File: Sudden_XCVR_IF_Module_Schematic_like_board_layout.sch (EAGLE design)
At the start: 31 parts, among them K1 REL-G5V1, K2 REL-G5V1, K3 RELAY-DPDT

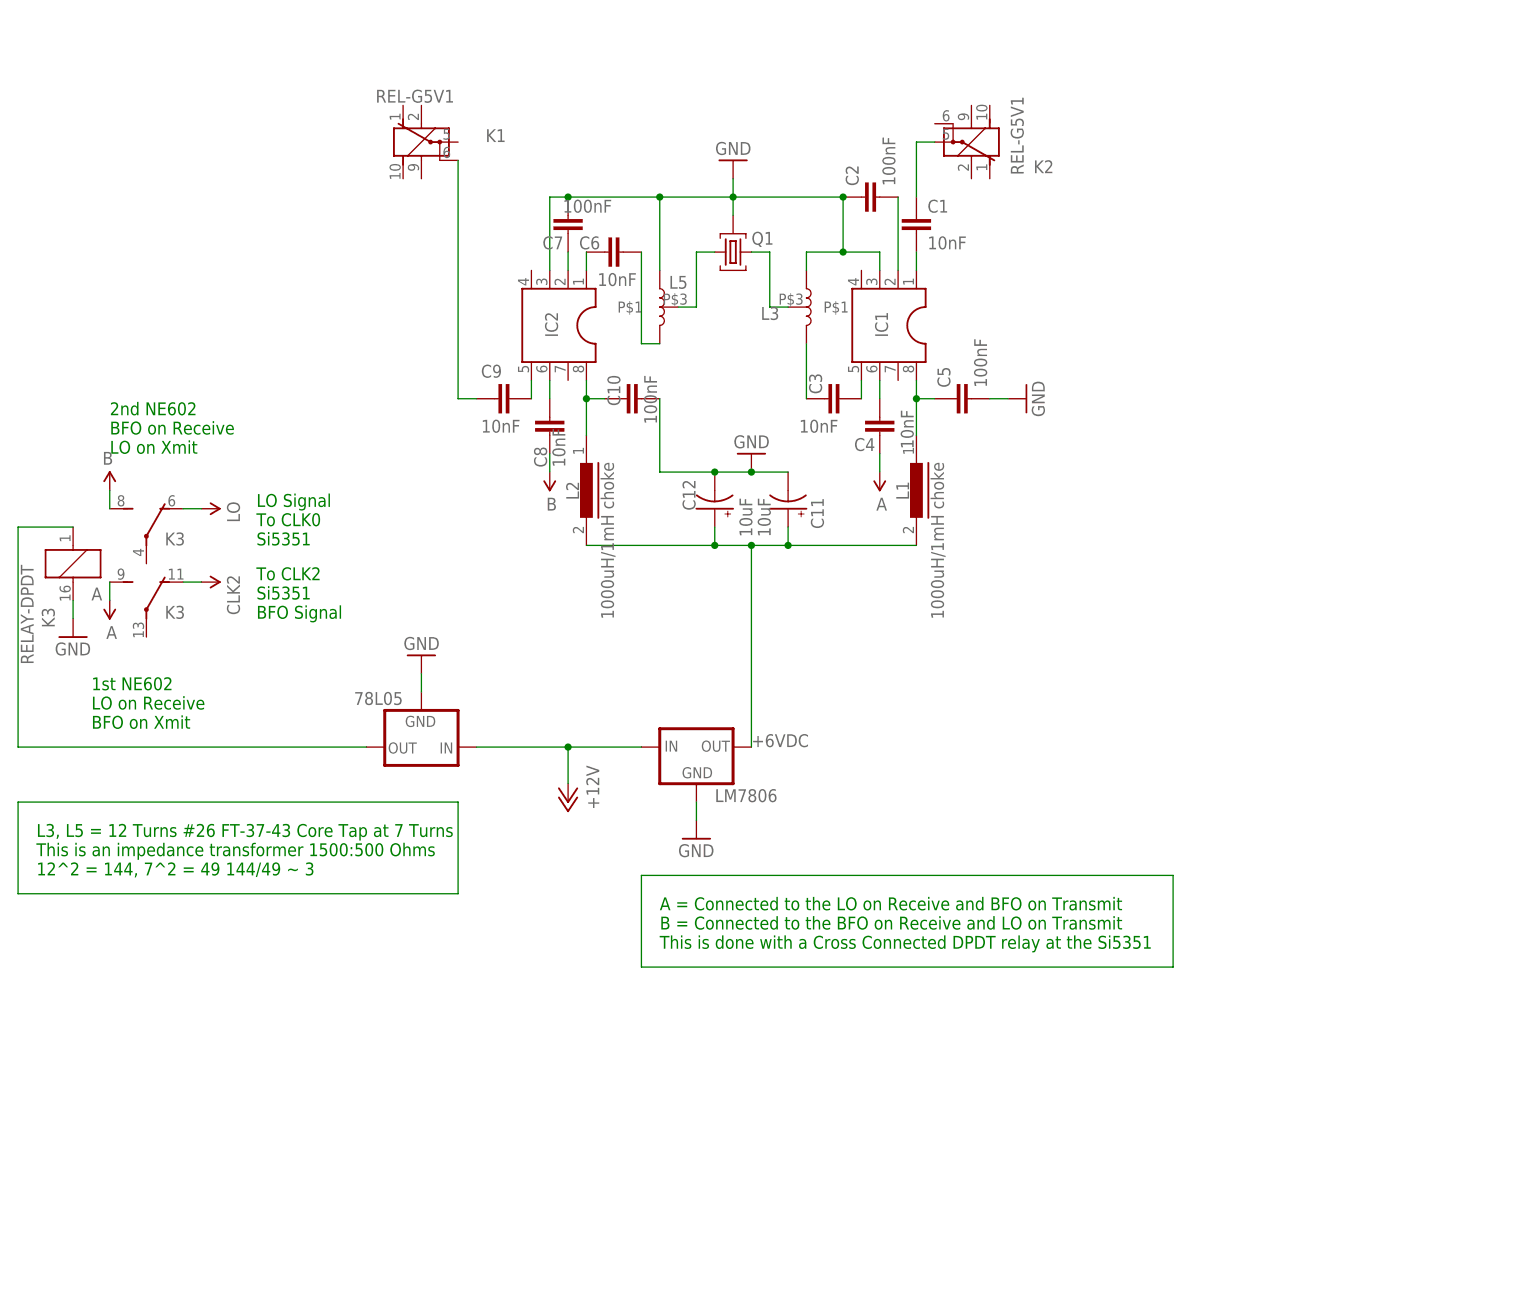
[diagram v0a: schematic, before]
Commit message: Added additional schematics and board layout
Added additional schmentics and board layout for Driver stage and a new IF schematic and board
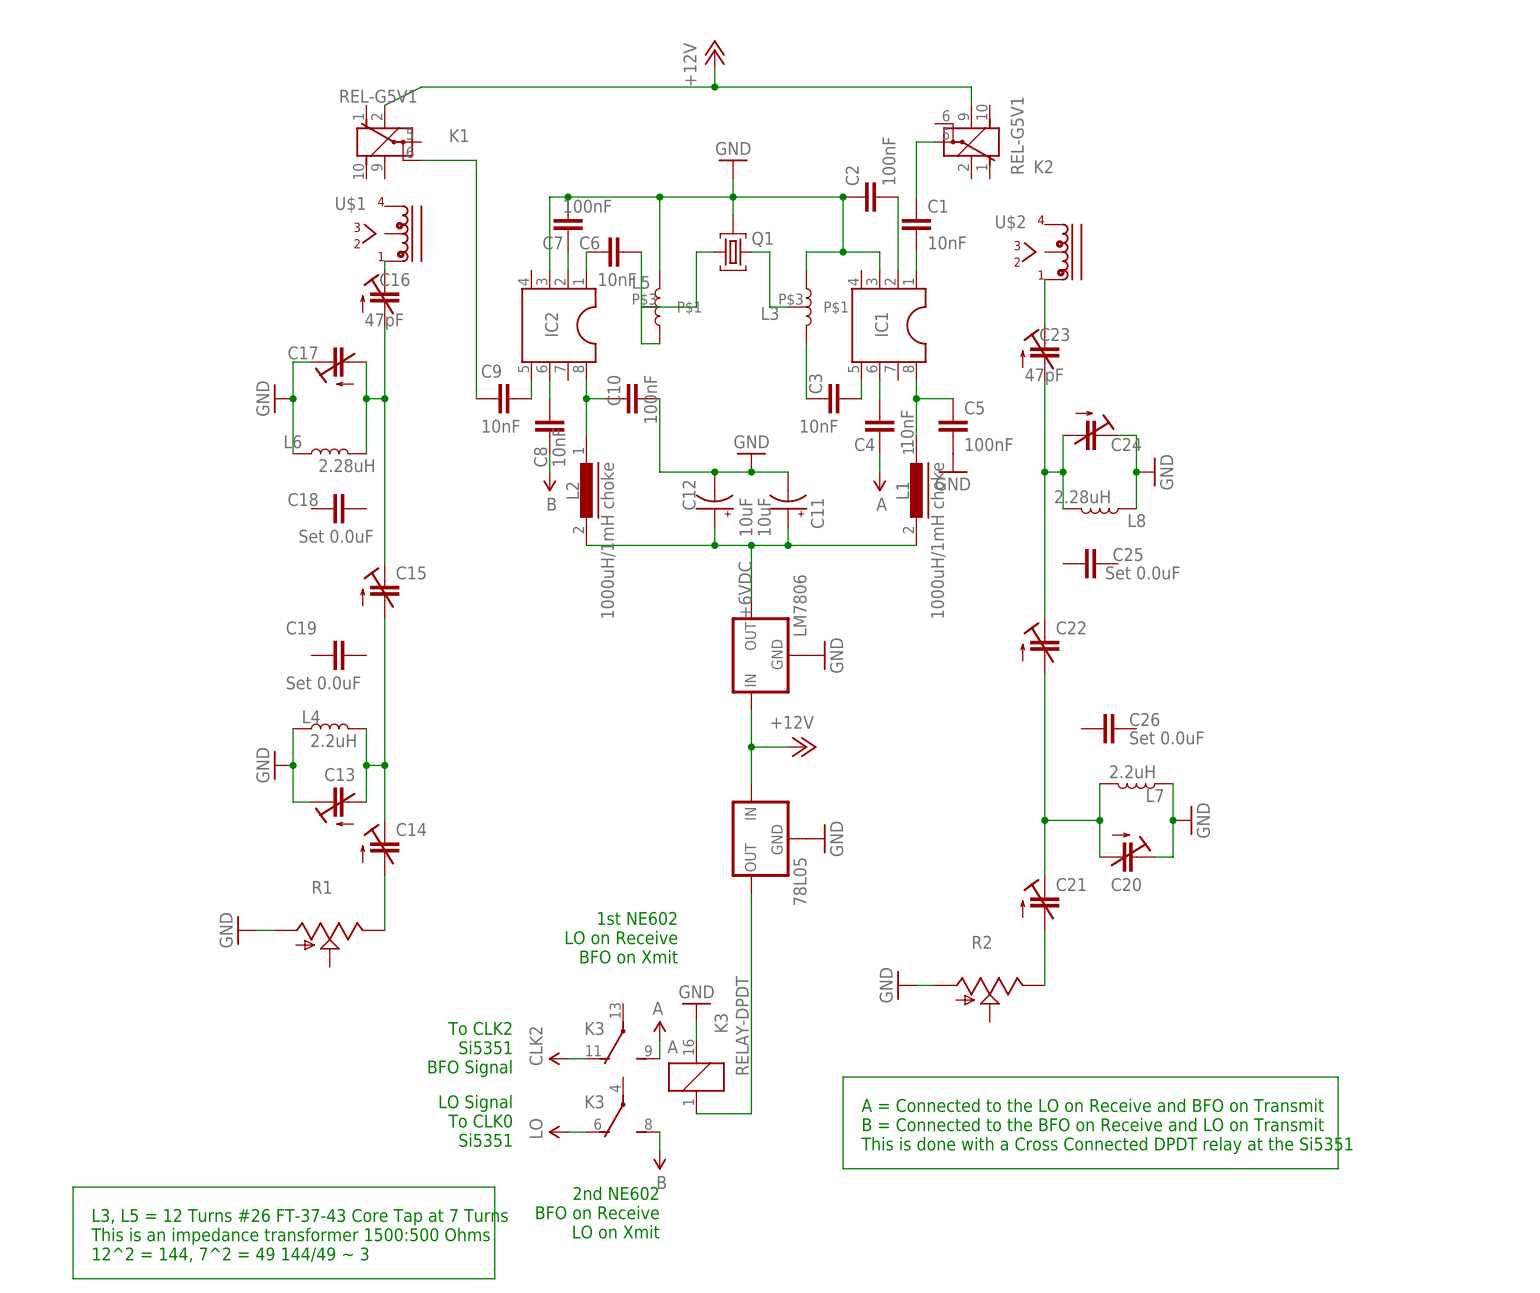
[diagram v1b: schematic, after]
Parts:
- added C13, C14, C15, C17, C20, C21, C22, C24: (no value), jim_muppet_parts:CAP-TRIMM3008
- added C16, C23: 47pF, jim_muppet_parts:CAP-TRIMM3008
- added C18, C19, C25, C26: Set 0.0uF, jim_muppet_parts:CAP-MEDIUM-MUPPET
- added L4, L7: 2.2uH, jim_muppet_parts:INDUCTOR-VLF4012AT-2.2UH
- added L6, L8: 2.28uH, jim_muppet_parts:INDUCTOR-VLF4012AT-2.2UH
- added P+2: +12V, jim_muppet_parts:+12V
- added R1, R2: (no value), jim_muppet_parts:POTENTIOMETER-TRIMCT6
- added U$1: T37-43_BIFILAR_TORIODBIFILAR-COIL/TRANSFORMER, jim_muppet_parts:T37-43_BIFILAR_TORIODBIFILAR-COIL/TRANSFORMER
- added U$2: BIFILAR_TORIOD, jim_muppet_parts:T37-43_BIFILAR_TORIODBIFILAR-COIL/TRANSFORMER
- L5: value INDUCTOR-TAPPED-MIRROREDINDUCTOR_TAPPED_MIRRORED -> INDUCTOR-TAPPED
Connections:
- new net N$21: C15.E, C16.A, C17.A, L6.2
- new net N$22: C14.A, R1.E
- new net N$23: C13.A, C14.E, C15.A, L4.2
- new net N$24: C23.E, U$2.C1A
- new net N$25: C22.E, C23.A, C24.A, L8.2
- new net N$26: C20.A, C21.E, C22.A, L7.2
- new net N$27: C21.A, R2.E
- new net N$8: C16.E, U$1.C1A
- net +12V: now also K11.1, K21.2, P+2.+12V
- net GND: now also C13.E, C17.E, C20.E, C24.E, L4.1, L6.1, L7.1, L8.1, R1.A, R2.A
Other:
- moved on the sheet: 78L05, C5, K1, K3, L5, LM7806

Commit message: Updated the IF module - mainly board layout
Updated the IF module - mainly board layout
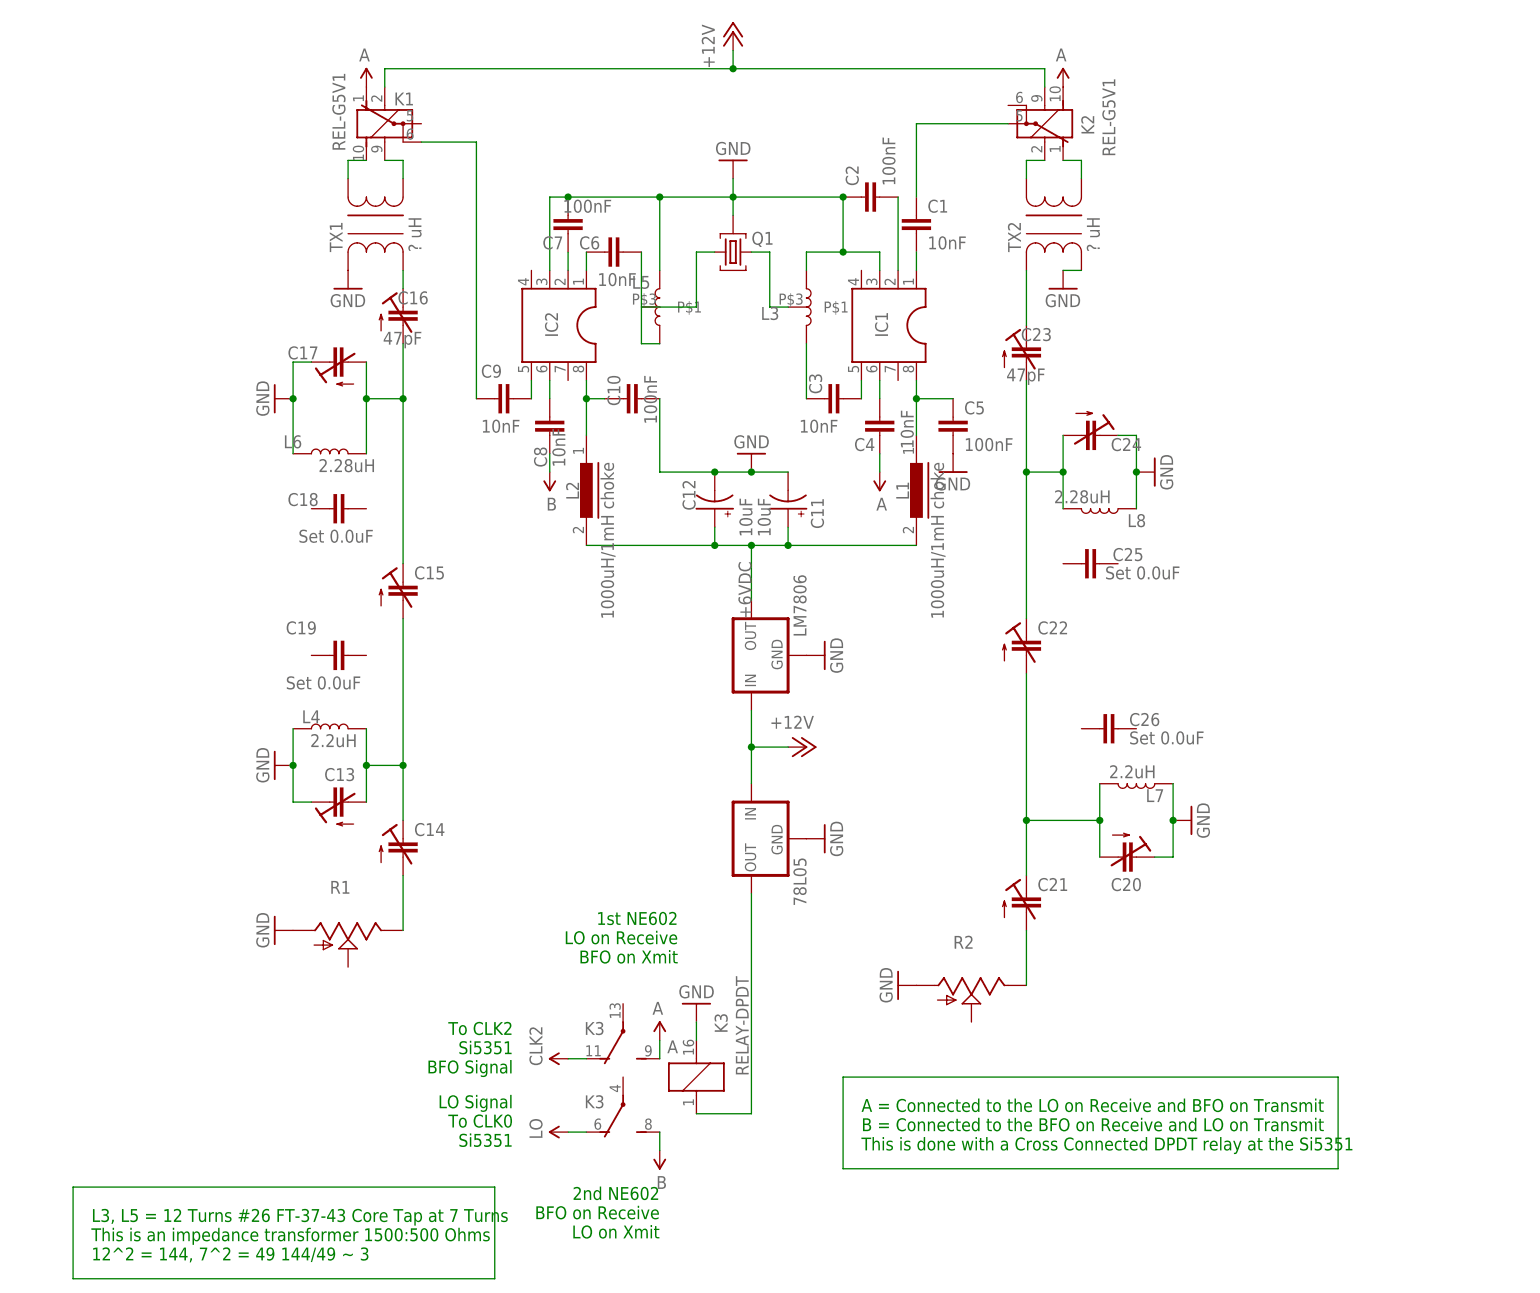
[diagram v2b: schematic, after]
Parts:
- removed U$1: T37-43_BIFILAR_TORIODBIFILAR-COIL/TRANSFORMER, jim_muppet_parts:T37-43_BIFILAR_TORIODBIFILAR-COIL/TRANSFORMER
- removed U$2: BIFILAR_TORIOD, jim_muppet_parts:T37-43_BIFILAR_TORIODBIFILAR-COIL/TRANSFORMER
- added A1, A2: A, jim_muppet_parts:VCC-IN
- added TX1, TX2: ? uH, jim_muppet_parts:TRANSFORMER_2WIRETRANSFORMER_2WIRE
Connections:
- new net N$28: K11.2, TX1.5
- new net N$29: K12.S, TX1.6
- new net N$30: K21.1, TX2.6
- new net N$31: K22.O, TX2.5
- net 3.3V: now also A1.3.3V, A2.3.3V, K12.O, K22.S
- net GND: now also TX1.2, TX2.1
- net N$24: now also TX2.2; no longer U$2.C1A
- net N$8: now also TX1.1; no longer U$1.C1A
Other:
- moved on the sheet: C14, C15, C16, C21, C22, C23, K1, K2, R1, R2
